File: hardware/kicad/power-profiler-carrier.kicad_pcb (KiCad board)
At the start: 4 copper layers, 160 x 100 mm, 309 parts, among them J1101 CPLD JTAG, J1201 Logic D0-D7, J201 JTAG, J202 3V3 GND, J301 USB-C power, J601 VIN, J801 VOUT, Q601 CSD17577Q3A, Q602 CSD17577Q3A, Q603 CSD17577Q3A, Q604 CSD17577Q3A, Q701 IRLML0030, Q702 IRLML0030, Q703 CSD17577Q3A, Q801 CSD17577Q3A, Q802 CSD17577Q3A, U1001 MCP6562-E/SN, U1002 MCP6561T-E/OT, U1101 EPM240T100C5N, U1201 SRV05-4, U1202 SRV05-4, U1203 SN74LVC8T245PW, U1301 MCP3208-BI/SL, U1302 MCP9700AT-E/TT, U201 ESP32-S3-DevKitC-1 N8R2/N16R2, U202 SN74LVC245APW, U301 LP5907MFX-3.3, U302 LP5907MFX-3.3, U401 LMR62014XMF, U402 LT3042EMSE, U403 LM27761DSG, U404 REF5025AID, U501 TPS63020DSJ, U502 OPA365AIDBV, U503 LT3080EDD, U504 MCP4921-E/SN, U505 OPA197IDBV, U601 TC4427EOA, U602 MCP6561T-E/OT, U701 TC4427EOA, U702 TC4427EOA, U703 MUX509IPWR, U801 OPA197IDBV, U901 AD8421ARZ, U902 OPA197IDBV, U903 OPA365AIDBV, U904 ADS8860IDGS

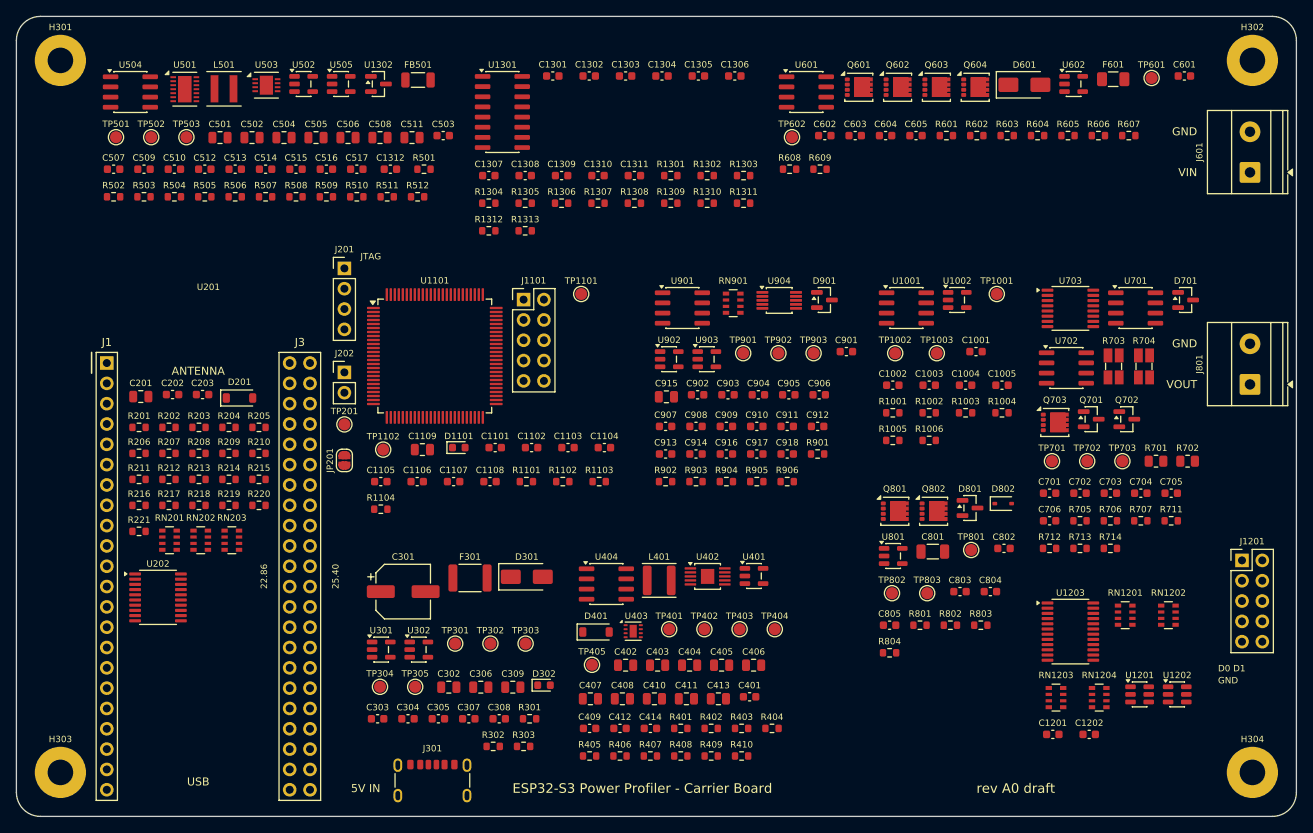
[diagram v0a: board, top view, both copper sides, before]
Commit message: feat(hardware): place the parts of draft A1 on a 130 mm x 100 mm board
The outline shrinks from 160 mm x 100 mm to 130 mm x 100 mm (D-46).
The back edge, on the left, has the Pico 2 with its USB connector and
the USB-C power connector. The front edge, on the right, has the logic
port and the two DUT connectors, each with the names of its pins.

The parts are no longer packed in rows. Each one stands near the pin
it serves, turned towards its connections, inside the area of its
functional block; the switching converters are in the left third and
the front end in the right third. The reference designators of 23
parts are hidden on the silkscreen, where no free place was left
beside the part, and three groups of parts lie just outside the
outline of their block.

Nothing is routed, and nobody has reviewed the placement for routing.
The design rules check reports no violation and no difference between
board and schematic; the unconnected items it lists are the missing
tracks.
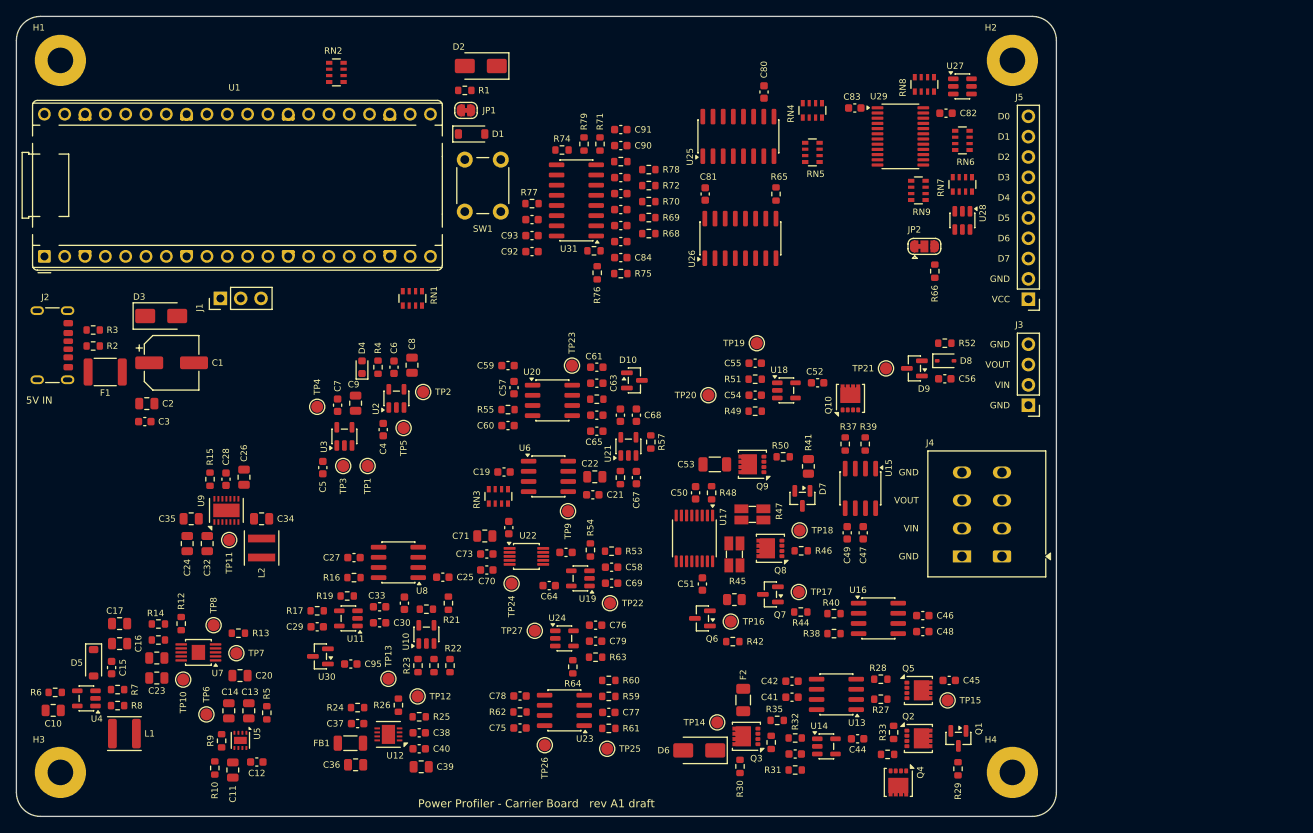
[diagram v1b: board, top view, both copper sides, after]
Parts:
- removed C1001, C1002, C1003, C1004, C1005, C1101, C1102, C1103, C1104, C1105, C1106, C1107, C1108, C1201, C1202, C1301, C1302, C1303, C1304, C1305, C1306, C1307, C1308, C1309, C1311, C1312, C202, C203, C303, C503, C507, C510, C512, C513, C514, C515, C516, C517, C602, C604, C702, C704, C705, C706, C802, C803, C804, C805, C901, C903, C909, C910, C913, C916: 100n, Capacitor_SMD:C_0603_1608Metric
- removed C1109, C201, C302, C306, C309, C413, C501, C502, C508, C511: 10u, Capacitor_SMD:C_0805_2012Metric
- removed C1310, C304, C305, C307, C308, C409, C414, C605, C904, C908, C917, C918: 1u, Capacitor_SMD:C_0603_1608Metric
- removed C301: 47u 16V, Capacitor_SMD:CP_Elec_6.3x5.4
- removed C401: 220p, Capacitor_SMD:C_0603_1608Metric
- removed C402, C405, C408, C410, C411: 4.7u, Capacitor_SMD:C_0805_2012Metric
- removed C403, C404, C406, C407: 4.7u 25V, Capacitor_SMD:C_0805_2012Metric
- removed C412, C509, C601, C701, C703, C902: 1u 25V, Capacitor_SMD:C_0603_1608Metric
- removed C504, C505, C506, C915: 22u, Capacitor_SMD:C_0805_2012Metric
- removed C603: 1n, Capacitor_SMD:C_0603_1608Metric
- removed C801: 100n C0G, Capacitor_SMD:C_1206_3216Metric
- removed C905: 1n C0G, Capacitor_SMD:C_0603_1608Metric
- removed C906, C907: 100p C0G, Capacitor_SMD:C_0603_1608Metric
- removed C911: 1.5n C0G, Capacitor_SMD:C_0603_1608Metric
- removed C912: 680p C0G, Capacitor_SMD:C_0603_1608Metric
- removed C914: 10n C0G, Capacitor_SMD:C_0603_1608Metric
- removed D1101: red, LED_SMD:LED_0603_1608Metric
- removed D201: B5819W, Diode_SMD:D_SOD-123
- removed D301: SMAJ5.0A, Diode_SMD:D_SMA
- removed D302: green, LED_SMD:LED_0603_1608Metric
- removed D401: MBR0530, Diode_SMD:D_SOD-123
- removed D601: SS34, Diode_SMD:D_SMA
- removed D701, D801, D901: BAV199, Package_TO_SOT_SMD:SOT-23
- removed D802: BZT52C5V6S, Diode_SMD:D_SOD-323
- removed F301: 2.5A hold, Fuse:Fuse_1812_4532Metric
- removed F601: 4A fast, Fuse:Fuse_1206_3216Metric
- removed FB501: 120R 3A, Inductor_SMD:L_1206_3216Metric
- removed H301, H302, H303, H304: M3, MountingHole:MountingHole_3.2mm_M3_Pad
- removed J1101: CPLD JTAG, Connector_PinHeader_2.54mm:PinHeader_2x05_P2.54mm_Vertical
- removed J1201: Logic D0-D7, Connector_PinHeader_2.54mm:PinHeader_2x05_P2.54mm_Vertical
- removed J201: JTAG, Connector_PinHeader_2.54mm:PinHeader_1x04_P2.54mm_Vertical
- removed J202: 3V3 GND, Connector_PinHeader_2.54mm:PinHeader_1x02_P2.54mm_Vertical
- removed J301: USB-C power, Connector_USB:USB_C_Receptacle_GCT_USB4125-xx-x_6P_TopMnt_Horizontal
- removed J601: VIN, TerminalBlock_Phoenix:TerminalBlock_Phoenix_MKDS-1,5-2-5.08_1x02_P5.08mm_Horizontal
- removed J801: VOUT, TerminalBlock_Phoenix:TerminalBlock_Phoenix_MKDS-1,5-2-5.08_1x02_P5.08mm_Horizontal
- removed JP201: 5V to devkit, Jumper:SolderJumper-2_P1.3mm_Open_RoundedPad1.0x1.5mm
- removed L401: 10u 1.3A, Inductor_SMD:L_Changjiang_FNR4020S
- removed L501: 1.5u 5A, Inductor_SMD:L_Coilcraft_XxL4020
- removed Q601, Q602, Q603, Q604, Q703, Q801, Q802: CSD17577Q3A, Package_SON:VSON-8_3.3x3.3mm_P0.65mm_NexFET
- removed Q701, Q702: IRLML0030, Package_TO_SOT_SMD:SOT-23
- removed R1001, R1004, R1005: 3.01k, Resistor_SMD:R_0603_1608Metric
- removed R1002, R1101, R1104, R1309, R206, R303, R508, R605, R606, R711, R712, R713, R714: 1k, Resistor_SMD:R_0603_1608Metric
- removed R1003: 34.8k, Resistor_SMD:R_0603_1608Metric
- removed R1006: 9.31k, Resistor_SMD:R_0603_1608Metric
- removed R1102, R1103, R1304, R1307, R1308, R1311, R217, R220, R221, R407, R510, R802, R803: 10k, Resistor_SMD:R_0603_1608Metric
- removed R1301, R1305, R607: 120k, Resistor_SMD:R_0603_1608Metric
- removed R1302, R1306, R1312, R210, R211, R212, R213, R214, R215, R216, R218, R219, R410, R608: 100k, Resistor_SMD:R_0603_1608Metric
- removed R1303: 110k, Resistor_SMD:R_0603_1608Metric
- removed R1310: 47k, Resistor_SMD:R_0603_1608Metric
- removed R1313: 200k, Resistor_SMD:R_0603_1608Metric
- removed R201, R202, R203, R204, R205, R207, R208, R209, R705, R706, R804: 47R, Resistor_SMD:R_0603_1608Metric
- removed R301, R302: 5.1k, Resistor_SMD:R_0603_1608Metric
- removed R401: 51k, Resistor_SMD:R_0603_1608Metric
- removed R402: 133k, Resistor_SMD:R_0603_1608Metric
- removed R403: 13.3k, Resistor_SMD:R_0603_1608Metric
- removed R404: 120k 0.1%, Resistor_SMD:R_0603_1608Metric
- removed R405: 442k, Resistor_SMD:R_0603_1608Metric
- removed R406: 12.4k, Resistor_SMD:R_0603_1608Metric
- removed R408: 2.2R, Resistor_SMD:R_0603_1608Metric
- removed R409: 226k, Resistor_SMD:R_0603_1608Metric
- removed R501: 470R, Resistor_SMD:R_0603_1608Metric
- removed R502, R505: 100k 0.1%, Resistor_SMD:R_0603_1608Metric
- removed R503: 121k 0.1%, Resistor_SMD:R_0603_1608Metric
- removed R504: 23.7k 0.1%, Resistor_SMD:R_0603_1608Metric
- removed R506: 20k 0.1%, Resistor_SMD:R_0603_1608Metric
- removed R507, R707: 10R, Resistor_SMD:R_0603_1608Metric
- removed R509: 4.3k, Resistor_SMD:R_0603_1608Metric
- removed R511: 10k 0.1%, Resistor_SMD:R_0603_1608Metric
- removed R512: 11k 0.1%, Resistor_SMD:R_0603_1608Metric
- removed R601, R603, R801, R906: 22R, Resistor_SMD:R_0603_1608Metric
- removed R602, R604: 1M, Resistor_SMD:R_0603_1608Metric
- removed R609: 2.2M, Resistor_SMD:R_0603_1608Metric
- removed R701: 1k 0.1%, Resistor_SMD:R_0805_2012Metric
- removed R702: 33R 0.1%, Resistor_SMD:R_0805_2012Metric
- removed R703: 1R 0.1%, Resistor_SMD:R_Shunt_Ohmite_LVK12
- removed R704: 0.1R 0.5%, Resistor_SMD:R_Shunt_Ohmite_LVK12
- removed R901: 523R 0.1%, Resistor_SMD:R_0603_1608Metric
- removed R902: 49.9k 0.1%, Resistor_SMD:R_0603_1608Metric
- removed R903: 1.02k 0.1%, Resistor_SMD:R_0603_1608Metric
- removed R904, R905: 3.9k, Resistor_SMD:R_0603_1608Metric
- removed RN1201, RN1202: 1k, Resistor_SMD:R_Array_Convex_4x0603
- removed RN1203, RN1204: 1M, Resistor_SMD:R_Array_Convex_4x0603
- removed RN201, RN202, RN203: 47R, Resistor_SMD:R_Array_Convex_4x0603
- removed RN901: 33R, Resistor_SMD:R_Array_Convex_4x0603
- removed TP1001: CMP_UP, TestPoint:TestPoint_Pad_D1.5mm
- removed TP1002: CMP_JUMP, TestPoint:TestPoint_Pad_D1.5mm
- removed TP1003: CMP_OC, TestPoint:TestPoint_Pad_D1.5mm
- removed TP1101: DBG0, TestPoint:TestPoint_Pad_D1.5mm
- removed TP1102: DBG1, TestPoint:TestPoint_Pad_D1.5mm
- removed TP201: +3V3_D, TestPoint:TestPoint_Pad_D1.5mm
- removed TP301: +5V, TestPoint:TestPoint_Pad_D1.5mm
- removed TP302: +3V3_C, TestPoint:TestPoint_Pad_D1.5mm
- removed TP303: +3V3_A, TestPoint:TestPoint_Pad_D1.5mm
- removed TP304, TP305, TP803: GND, TestPoint:TestPoint_Pad_D1.5mm
- removed TP401: +13V5, TestPoint:TestPoint_Pad_D1.5mm
- removed TP402: +12V_A, TestPoint:TestPoint_Pad_D1.5mm
- removed TP403: -4V_A, TestPoint:TestPoint_Pad_D1.5mm
- removed TP404: VREF, TestPoint:TestPoint_Pad_D1.5mm
- removed TP405: PWR_GOOD, TestPoint:TestPoint_Pad_D1.5mm
- removed TP501: V_PRE, TestPoint:TestPoint_Pad_D1.5mm
- removed TP502: LDO_OUT, TestPoint:TestPoint_Pad_D1.5mm
- removed TP503: LDO_SET, TestPoint:TestPoint_Pad_D1.5mm
- removed TP601: SUPPLY, TestPoint:TestPoint_Pad_D1.5mm
- removed TP602: VIN_P, TestPoint:TestPoint_Pad_D1.5mm
- removed TP701: G_R1, TestPoint:TestPoint_Pad_D1.5mm
- removed TP702: G_R2, TestPoint:TestPoint_Pad_D1.5mm
- removed TP703: G_R3, TestPoint:TestPoint_Pad_D1.5mm
- removed TP801: VOUT, TestPoint:TestPoint_Pad_D1.5mm
- removed TP802: GUARD, TestPoint:TestPoint_Pad_D1.5mm
- removed TP901: AMP_RAW, TestPoint:TestPoint_Pad_D1.5mm
- removed TP902: ADC_IN, TestPoint:TestPoint_Pad_D1.5mm
- removed TP903: PED, TestPoint:TestPoint_Pad_D1.5mm
- removed U1001: MCP6562-E/SN, Package_SO:SOIC-8_3.9x4.9mm_P1.27mm
- removed U1002, U602: MCP6561T-E/OT, Package_TO_SOT_SMD:SOT-23-5
- removed U1101: EPM240T100C5N, Package_QFP:LQFP-100_14x14mm_P0.5mm
- removed U1201, U1202: SRV05-4, Package_TO_SOT_SMD:SOT-23-6
- removed U1203: SN74LVC8T245PW, Package_SO:TSSOP-24_4.4x7.8mm_P0.65mm
- removed U1301: MCP3208-BI/SL, Package_SO:SOIC-16_3.9x9.9mm_P1.27mm
- removed U1302: MCP9700AT-E/TT, Package_TO_SOT_SMD:SOT-23
- removed U201: ESP32-S3-DevKitC-1 N8R2/N16R2, PowerProfiler:ESP32-S3-DevKitC-1_Socket
- removed U202: SN74LVC245APW, Package_SO:TSSOP-20_4.4x6.5mm_P0.65mm
- removed U301, U302: LP5907MFX-3.3, Package_TO_SOT_SMD:SOT-23-5
- removed U401: LMR62014XMF, Package_TO_SOT_SMD:SOT-23-5
- removed U402: LT3042EMSE, Package_SO:MSOP-10-1EP_3x3mm_P0.5mm_EP1.68x1.88mm
- removed U403: LM27761DSG, Package_SON:WSON-8-1EP_2x2mm_P0.5mm_EP0.9x1.6mm
- removed U404: REF5025AID, Package_SO:SOIC-8_3.9x4.9mm_P1.27mm
- removed U501: TPS63020DSJ, Package_DFN_QFN:DFN-14-1EP_3x4mm_P0.5mm_EP1.7x3.3mm
- removed U502, U903: OPA365AIDBV, Package_TO_SOT_SMD:SOT-23-5
- removed U503: LT3080EDD, Package_DFN_QFN:DFN-8-1EP_3x3mm_P0.5mm_EP1.66x2.38mm
- removed U504: MCP4921-E/SN, Package_SO:SOIC-8_3.9x4.9mm_P1.27mm
- removed U505, U801, U902: OPA197IDBV, Package_TO_SOT_SMD:SOT-23-5
- removed U601, U701, U702: TC4427EOA, Package_SO:SOIC-8_3.9x4.9mm_P1.27mm
- removed U703: MUX509IPWR, Package_SO:TSSOP-16_4.4x5mm_P0.65mm
- removed U901: AD8421ARZ, Package_SO:SOIC-8_3.9x4.9mm_P1.27mm
- removed U904: ADS8860IDGS, Package_SO:MSOP-10_3x3mm_P0.5mm
- added C1: 47u 16V, Capacitor_SMD:CP_Elec_6.3x5.4, F.Cu at (69.4, 93.3)
- added C10: 4.7u, Capacitor_SMD:C_0805_2012Metric, F.Cu at (54.6, 136.8)
- added C11: 4.7u, Capacitor_SMD:C_0805_2012Metric, F.Cu at (77.0, 144.2)
- added C12: 1u, Capacitor_SMD:C_0603_1608Metric, F.Cu at (80.0, 143.2)
- added C13: 4.7u, Capacitor_SMD:C_0805_2012Metric, F.Cu at (79.0, 136.8)
- added C14: 4.7u, Capacitor_SMD:C_0805_2012Metric, F.Cu at (76.5, 136.8)
- added C15: 220p, Capacitor_SMD:C_0603_1608Metric, F.Cu at (61.9, 131.4)
- added C16: 4.7u 25V, Capacitor_SMD:C_0805_2012Metric, F.Cu at (62.9, 128.4)
- added C17: 4.7u 25V, Capacitor_SMD:C_0805_2012Metric, F.Cu at (62.9, 125.9)
- added C18: 4.7u, Capacitor_SMD:C_0805_2012Metric, F.Cu at (67.5, 130.2)
- added C19: 1u 25V, Capacitor_SMD:C_0603_1608Metric, F.Cu at (111.0, 107.0)
- added C2: 10u, Capacitor_SMD:C_0805_2012Metric, F.Cu at (66.3, 98.4)
- added C20: 4.7u 25V, Capacitor_SMD:C_0805_2012Metric, F.Cu at (78.0, 132.4)
- added C21: 1u, Capacitor_SMD:C_0603_1608Metric, F.Cu at (122.0, 109.8)
- added C22: 10u, Capacitor_SMD:C_0805_2012Metric, F.Cu at (122.3, 107.5)
- added C23: 4.7u 25V, Capacitor_SMD:C_0805_2012Metric, F.Cu at (67.5, 132.7)
- added C24: 10u, Capacitor_SMD:C_0805_2012Metric, F.Cu at (71.3, 115.9)
- added C25: 100n, Capacitor_SMD:C_0603_1608Metric, F.Cu at (103.3, 120.1)
- added C26: 10u, Capacitor_SMD:C_0805_2012Metric, F.Cu at (78.5, 107.6)
- added C27: 100n, Capacitor_SMD:C_0603_1608Metric, F.Cu at (92.2, 117.7)
- added C28: 100n, Capacitor_SMD:C_0603_1608Metric, F.Cu at (76.2, 107.8)
- added C29: 100n, Capacitor_SMD:C_0603_1608Metric, F.Cu at (87.6, 126.3)
- added C3: 100n, Capacitor_SMD:C_0603_1608Metric, F.Cu at (66.0, 100.7)
- added C30: 100n, Capacitor_SMD:C_0603_1608Metric, F.Cu at (95.4, 125.8)
- added C31: 100n, Capacitor_SMD:C_0603_1608Metric, F.Cu at (98.5, 123.3)
- added C32: 22u, Capacitor_SMD:C_0805_2012Metric, F.Cu at (73.8, 115.9)
- added C33: 100n, Capacitor_SMD:C_0603_1608Metric, F.Cu at (95.4, 123.8)
- added C34: 22u, Capacitor_SMD:C_0805_2012Metric, F.Cu at (80.7, 112.8)
- added C35: 22u, Capacitor_SMD:C_0805_2012Metric, F.Cu at (71.8, 112.8)
- added C36: 10u, Capacitor_SMD:C_0805_2012Metric, F.Cu at (92.4, 143.6)
- added C37: 1u 25V, Capacitor_SMD:C_0603_1608Metric, F.Cu at (92.7, 138.4)
- added C38: 100n, Capacitor_SMD:C_0603_1608Metric, F.Cu at (100.3, 139.6)
- added C39: 10u, Capacitor_SMD:C_0805_2012Metric, F.Cu at (100.6, 143.8)
- added C4: 1u, Capacitor_SMD:C_0603_1608Metric, F.Cu at (95.8, 101.7)
- added C40: 100n, Capacitor_SMD:C_0603_1608Metric, F.Cu at (100.3, 141.6)
- added C41: 1u 25V, Capacitor_SMD:C_0603_1608Metric, F.Cu at (146.9, 135.1)
- added C42: 100n, Capacitor_SMD:C_0603_1608Metric, F.Cu at (146.9, 133.1)
- added C43: 1n, Capacitor_SMD:C_0603_1608Metric, F.Cu at (147.3, 142.2)
- added C44: 100n, Capacitor_SMD:C_0603_1608Metric, F.Cu at (155.2, 140.3)
- added C45: 1u, Capacitor_SMD:C_0603_1608Metric, F.Cu at (166.6, 133.0)
- added C46: 1u 25V, Capacitor_SMD:C_0603_1608Metric, F.Cu at (163.3, 124.9)
- added C47: 100n, Capacitor_SMD:C_0603_1608Metric, F.Cu at (155.8, 114.5)
- added C48: 1u 25V, Capacitor_SMD:C_0603_1608Metric, F.Cu at (163.3, 126.9)
- added C49: 100n, Capacitor_SMD:C_0603_1608Metric, F.Cu at (153.8, 114.5)
- added C5: 1u, Capacitor_SMD:C_0603_1608Metric, F.Cu at (88.3, 106.4)
- added C50: 100n, Capacitor_SMD:C_0603_1608Metric, F.Cu at (134.9, 109.5)
- added C51: 100n, Capacitor_SMD:C_0603_1608Metric, F.Cu at (135.8, 121.0)
- added C52: 100n, Capacitor_SMD:C_0603_1608Metric, F.Cu at (150.2, 95.8)
- added C53: 100n C0G, Capacitor_SMD:C_1206_3216Metric, F.Cu at (137.3, 106.0)
- added C54: 100n, Capacitor_SMD:C_0603_1608Metric, F.Cu at (142.3, 97.3)
- added C55: 100n, Capacitor_SMD:C_0603_1608Metric, F.Cu at (142.3, 93.3)
- added C56: 100n, Capacitor_SMD:C_0603_1608Metric, F.Cu at (166.1, 95.3)
- added C57: 1n C0G, Capacitor_SMD:C_0603_1608Metric, F.Cu at (112.2, 96.4)
- added C58: 1u, Capacitor_SMD:C_0603_1608Metric, F.Cu at (124.4, 118.8)
- added C59: 100p C0G, Capacitor_SMD:C_0603_1608Metric, F.Cu at (111.5, 93.7)
- added C6: 1u, Capacitor_SMD:C_0603_1608Metric, F.Cu at (97.2, 93.8)
- added C60: 100p C0G, Capacitor_SMD:C_0603_1608Metric, F.Cu at (111.5, 101.2)
- added C61: 100n, Capacitor_SMD:C_0603_1608Metric, F.Cu at (122.5, 93.8)
- added C62: 100n, Capacitor_SMD:C_0603_1608Metric, F.Cu at (122.5, 99.8)
- added C63: 1u 25V, Capacitor_SMD:C_0603_1608Metric, F.Cu at (122.5, 95.8)
- added C64: 100n, Capacitor_SMD:C_0603_1608Metric, F.Cu at (116.6, 121.2)
- added C65: 1u, Capacitor_SMD:C_0603_1608Metric, F.Cu at (122.5, 101.8)
- added C66: 100n, Capacitor_SMD:C_0603_1608Metric, F.Cu at (125.5, 99.8)
- added C67: 680p C0G, Capacitor_SMD:C_0603_1608Metric, F.Cu at (127.5, 107.7)
- added C68: 1.5n C0G, Capacitor_SMD:C_0603_1608Metric, F.Cu at (127.5, 99.8)
- added C69: 100n, Capacitor_SMD:C_0603_1608Metric, F.Cu at (124.4, 120.8)
- added C7: 1u, Capacitor_SMD:C_0603_1608Metric, F.Cu at (90.2, 98.6)
- added C70: 10n C0G, Capacitor_SMD:C_0603_1608Metric, F.Cu at (108.8, 119.2)
- added C71: 22u, Capacitor_SMD:C_0805_2012Metric, F.Cu at (108.5, 115.0)
- added C72: 100n, Capacitor_SMD:C_0603_1608Metric, F.Cu at (111.5, 113.9)
- added C73: 1u, Capacitor_SMD:C_0603_1608Metric, F.Cu at (108.8, 117.2)
- added C74: 1u, Capacitor_SMD:C_0603_1608Metric, F.Cu at (118.7, 117.0)
- added C75: 100n, Capacitor_SMD:C_0603_1608Metric, F.Cu at (113.0, 138.9)
- added C76: 100n, Capacitor_SMD:C_0603_1608Metric, F.Cu at (122.4, 126.1)
- added C77: 100n, Capacitor_SMD:C_0603_1608Metric, F.Cu at (124.0, 137.0)
- added C78: 100n, Capacitor_SMD:C_0603_1608Metric, F.Cu at (113.0, 134.9)
- added C79: 100n, Capacitor_SMD:C_0603_1608Metric, F.Cu at (122.4, 128.1)
- added C8: 10u, Capacitor_SMD:C_0805_2012Metric, F.Cu at (99.5, 93.6)
- added C80: 100n, Capacitor_SMD:C_0603_1608Metric, F.Cu at (143.4, 59.5)
- added C81: 100n, Capacitor_SMD:C_0603_1608Metric, F.Cu at (136.1, 72.2)
- added C82: 100n, Capacitor_SMD:C_0603_1608Metric, F.Cu at (166.2, 62.1)
- added C83: 100n, Capacitor_SMD:C_0603_1608Metric, F.Cu at (154.8, 61.5)
- added C84: 100n, Capacitor_SMD:C_0603_1608Metric, F.Cu at (125.5, 80.2)
- added C85: 100n, Capacitor_SMD:C_0603_1608Metric, F.Cu at (125.5, 78.2)
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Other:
- board size 160 x 100 mm -> 130 x 100 mm
- board text added: "Controller"
- board text added: "D0"
- board text added: "D1"
- board text added: "D2"
- board text added: "D3"
- board text added: "D4"
- board text added: "D5"
- board text added: "D6"
- board text added: "D7"
- board text added: "Logic inputs"
- board text added: "Mode switches"
- board text added: "Power Profiler - Carrier Board rev A1 draft"
- board text added: "Pre-regulator"
- board text added: "Side data"
- board text added: "VCC"
- board text removed: "D0 D1"
- board text removed: "Digital inputs"
- board text removed: "ESP32-S3 Power Profiler - Carrier Board"
- board text removed: "JTAG"
- board text removed: "Path switching"
- board text removed: "Range logic"
- board text removed: "rev A0 draft"

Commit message: feat(hardware): place and route draft A2 on a 150 mm x 100 mm board
The outline grows from 130 mm x 100 mm to 150 mm x 100 mm (D-85). A
script places the 425 footprints inside the areas of sixteen functional
blocks, with the front end under the frame of a shield can, and an
autorouter draws the tracks (D-86): 956 of the 984 connections, on
three layers over an unbroken ground plane. 28 connections are open.

The project file holds thirteen net classes, the default class among
them, and a rule file adds the clearances that a net class cannot
express. The stackup is the build that section 10.1 of the
specification assumes until a manufacturer is chosen.

The design rules check reports no rule violation and no difference
between board and schematic; its 28 unconnected items are the open
connections. The board is an autorouted draft that needs a layout
review before fabrication: the pours of the 1 A path, the guard ring,
the sense pairs and the loops of the switching converters are not
drawn.
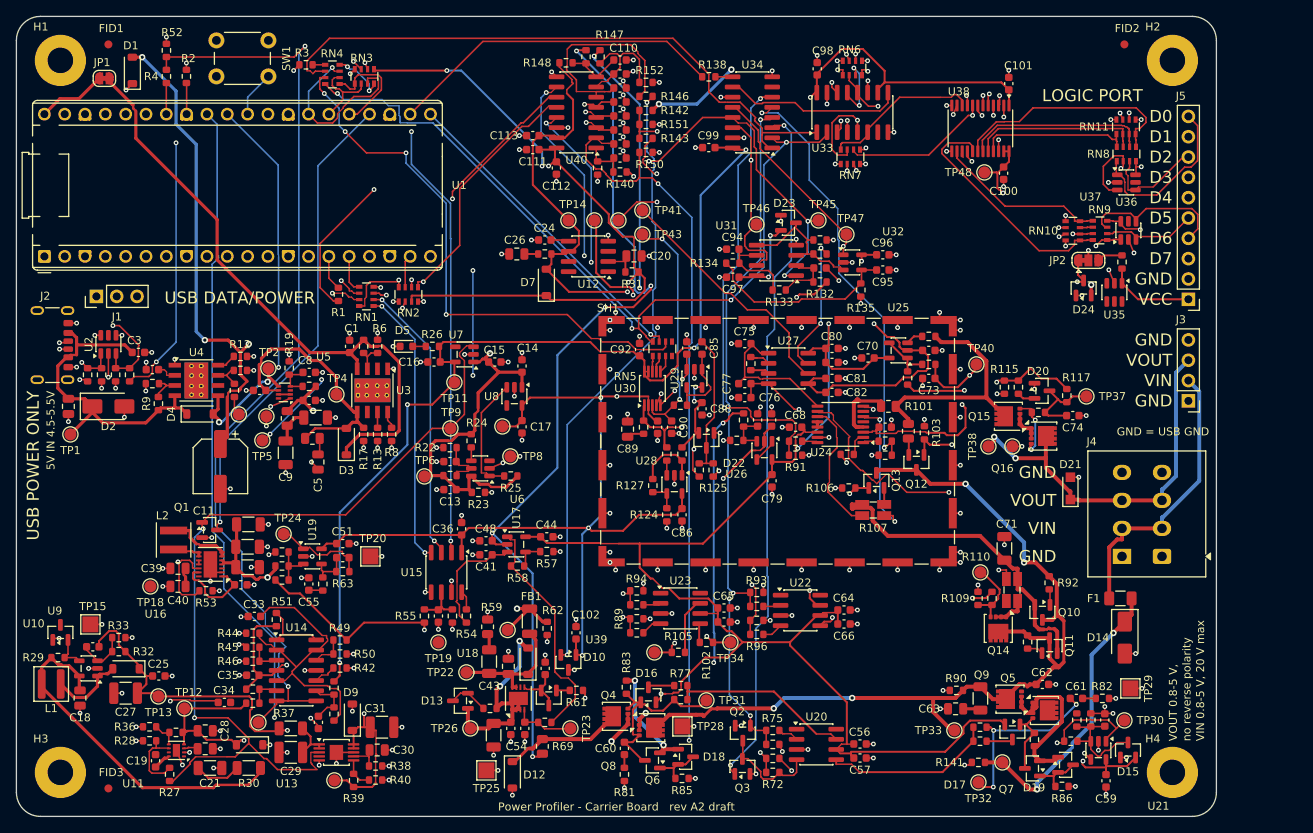
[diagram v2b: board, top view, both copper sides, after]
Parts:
- removed F2: 4A fast, Fuse:Fuse_1206_3216Metric
- added C100: 100n 50V X7R, Capacitor_SMD:C_0603_1608Metric, F.Cu at (173.4, 69.6)
- added C101: 100n 50V X7R, Capacitor_SMD:C_0603_1608Metric, F.Cu at (174.1, 58.4)
- added C102: 100n 50V X7R, Capacitor_SMD:C_0603_1608Metric, F.Cu at (120.0, 127.0)
- added C103: 100n 50V X7R, Capacitor_SMD:C_0603_1608Metric, F.Cu at (125.5, 67.7)
- added C104: 100n 50V X7R, Capacitor_SMD:C_0603_1608Metric, F.Cu at (125.5, 66.0)
- added C105: 100n 50V X7R, Capacitor_SMD:C_0603_1608Metric, F.Cu at (125.5, 64.2)
- added C106: 100n 50V X7R, Capacitor_SMD:C_0603_1608Metric, F.Cu at (125.5, 62.5)
- added C107: 100n 50V X7R, Capacitor_SMD:C_0603_1608Metric, F.Cu at (125.5, 60.7)
- added C108: 100n 50V X7R, Capacitor_SMD:C_0603_1608Metric, F.Cu at (125.5, 59.0)
- added C109: 100n 50V X7R, Capacitor_SMD:C_0603_1608Metric, F.Cu at (125.5, 57.2)
- added C110: 100n 50V X7R, Capacitor_SMD:C_0603_1608Metric, F.Cu at (125.5, 55.5)
- added C111: 100n 50V X7R, Capacitor_SMD:C_0603_1608Metric, F.Cu at (114.5, 66.7)
- added C112: 1u 25V X7R, Capacitor_SMD:C_0603_1608Metric, F.Cu at (117.5, 69.0)
- added C113: 100n 50V X7R, Capacitor_SMD:C_0603_1608Metric, F.Cu at (114.5, 64.9)
- added C96: 100n 50V X7R, Capacitor_SMD:C_0603_1608Metric, F.Cu at (158.3, 79.8)
- added C97: 100n 50V X7R, Capacitor_SMD:C_0603_1608Metric, F.Cu at (139.6, 82.6)
- added C98: 100n 50V X7R, Capacitor_SMD:C_0603_1608Metric, F.Cu at (150.1, 56.5)
- added C99: 100n 50V X7R, Capacitor_SMD:C_0603_1608Metric, F.Cu at (136.6, 66.4)
- added D11: 1N5819HW, Diode_SMD:D_SOD-123, F.Cu at (114.0, 130.6)
- added D12: 1N5819HW, Diode_SMD:D_SOD-123, F.Cu at (112.0, 144.8)
- added D13: BAV199, Package_TO_SOT_SMD:SOT-23, F.Cu at (105.5, 135.6)
- added D14: SMAJ20CA, Diode_SMD:D_SMA, F.Cu at (188.6, 127.7)
- added D15: BAV199, Package_TO_SOT_SMD:SOT-23, F.Cu at (188.9, 141.7)
- added D16: BAV199, Package_TO_SOT_SMD:SOT-23, F.Cu at (129.0, 134.8)
- added D17: BAV199, Package_TO_SOT_SMD:SOT-23, F.Cu at (174.5, 139.4)
- added D18: BAV199, Package_TO_SOT_SMD:SOT-23, F.Cu at (133.7, 142.6)
- added D19: BAV199, Package_TO_SOT_SMD:SOT-23, F.Cu at (181.2, 143.6)
- added D20: BAV199, Package_TO_SOT_SMD:SOT-23, F.Cu at (178.2, 96.8)
- added D21: PTVS15VS1UR, Diode_SMD:Nexperia_CFP3_SOD-123W, F.Cu at (181.8, 109.0)
- added D22: BAV199, Package_TO_SOT_SMD:SOT-23, F.Cu at (136.2, 103.0)
- added D23: BAV199, Package_TO_SOT_SMD:SOT-23, F.Cu at (146.5, 75.8)
- added D24: BAT54S, Package_TO_SOT_SMD:SOT-23, F.Cu at (183.4, 84.0)
- added FID1: Fiducial, Fiducial:Fiducial_1mm_Mask2mm, F.Cu at (61.5, 53.5)
- added FID2: Fiducial, Fiducial:Fiducial_1mm_Mask2mm, F.Cu at (188.5, 53.5)
- added FID3: Fiducial, Fiducial:Fiducial_1mm_Mask2mm, F.Cu at (61.5, 146.5)
- added Q11: IRLML0030, Package_TO_SOT_SMD:SOT-23, F.Cu at (179.2, 128.7)
- added Q12: IRLML0030, Package_TO_SOT_SMD:SOT-23, F.Cu at (162.5, 105.8)
- added Q13: IRLML0030, Package_TO_SOT_SMD:SOT-23, F.Cu at (157.5, 108.0)
- added Q14: CSD17577Q3A, Package_SON:VSON-8_3.3x3.3mm_P0.65mm_NexFET, F.Cu at (172.8, 126.5)
- added Q15: CSD17577Q3A, Package_SON:VSON-8_3.3x3.3mm_P0.65mm_NexFET, F.Cu at (174.0, 100.0)
- added Q16: CSD17577Q3A, Package_SON:VSON-8_3.3x3.3mm_P0.65mm_NexFET, F.Cu at (178.3, 102.5)
- added R100: 22R 1%, Resistor_SMD:R_0603_1608Metric, F.Cu at (176.4, 128.2)
- added R101: 1k 0.1% 25ppm, Resistor_SMD:R_0805_2012Metric, F.Cu at (159.0, 98.8)
- added R102: 47R 1%, Resistor_SMD:R_0603_1608Metric, F.Cu at (136.2, 128.2)
- added R103: 100k 1%, Resistor_SMD:R_0603_1608Metric, F.Cu at (163.5, 102.0)
- added R104: 33R 0.1% 25ppm, Resistor_SMD:R_0805_2012Metric, F.Cu at (161.5, 101.8)
- added R105: 47R 1%, Resistor_SMD:R_0603_1608Metric, F.Cu at (132.8, 129.5)
- added R106: 100k 1%, Resistor_SMD:R_0603_1608Metric, F.Cu at (154.1, 109.0)
- added R107: 1R 0.5% 25ppm, Resistor_SMD:R_Shunt_Ohmite_LVK12, F.Cu at (157.1, 111.7)
- added R108: 10R 1%, Resistor_SMD:R_0603_1608Metric, F.Cu at (171.9, 122.8)
- added R109: 100k 1%, Resistor_SMD:R_0603_1608Metric, F.Cu at (170.2, 122.8)
- added R110: 0.1R 0.25% 50ppm, Resistor_SMD:R_Shunt_Ohmite_LVK12, F.Cu at (174.4, 121.7)
- added R111: 1k 1%, Resistor_SMD:R_0603_1608Metric, F.Cu at (147.4, 103.1)
- added R112: 1k 1%, Resistor_SMD:R_0603_1608Metric, F.Cu at (158.6, 103.1)
- added R113: 10k 1%, Resistor_SMD:R_0603_1608Metric, F.Cu at (153.8, 104.8)
- added R114: 10k 1%, Resistor_SMD:R_0603_1608Metric, F.Cu at (164.1, 90.0)
- added R115: 100k 1%, Resistor_SMD:R_0603_1608Metric, F.Cu at (173.5, 96.3)
- added R116: 220R 1%, Resistor_SMD:R_0603_1608Metric, F.Cu at (175.2, 96.3)
- added R117: 2.2M 1%, Resistor_SMD:R_0603_1608Metric, F.Cu at (181.3, 97.4)
- added R118: 1k 1%, Resistor_SMD:R_0603_1608Metric, F.Cu at (161.4, 95.2)
- added R119: 47R 1%, Resistor_SMD:R_0603_1608Metric, F.Cu at (164.1, 93.5)
- added R120: 10R 1%, Resistor_SMD:R_0603_1608Metric, F.Cu at (177.8, 99.5)
- added R121: 49.9k 0.1% 25ppm, Resistor_SMD:R_0603_1608Metric, F.Cu at (140.9, 100.5)
- added R122: 1.02k 0.1% 25ppm, Resistor_SMD:R_0603_1608Metric, F.Cu at (140.1, 103.0)
- added R123: 523R 0.1% 25ppm, Resistor_SMD:R_0603_1608Metric, F.Cu at (141.8, 93.4)
- added R124: 11k 0.1% 25ppm, Resistor_SMD:R_0603_1608Metric, F.Cu at (131.3, 112.3)
- added R125: 3.9k 1%, Resistor_SMD:R_0603_1608Metric, F.Cu at (137.1, 106.7)
- added R126: 10k 1%, Resistor_SMD:R_0603_1608Metric, F.Cu at (131.3, 104.7)
- added R127: 1k 0.1% 25ppm, Resistor_SMD:R_0603_1608Metric, F.Cu at (129.6, 108.7)
- added R128: 3.9k 1%, Resistor_SMD:R_0603_1608Metric, F.Cu at (135.3, 106.7)
- added R129: 10R 1%, Resistor_SMD:R_0603_1608Metric, F.Cu at (133.2, 104.7)
- added R130: 22R 1%, Resistor_SMD:R_0603_1608Metric, F.Cu at (133.0, 98.6)
- added R131: 0.22R 1%, Resistor_SMD:R_0603_1608Metric, F.Cu at (128.4, 101.3)
- added R132: 34.8k 0.1% 25ppm, Resistor_SMD:R_0603_1608Metric, F.Cu at (150.4, 83.2)
- added R133: 3.6k 0.1% 25ppm, Resistor_SMD:R_0603_1608Metric, F.Cu at (145.3, 84.2)
- added R134: 2.4k 0.1% 25ppm, Resistor_SMD:R_0603_1608Metric, F.Cu at (139.6, 80.8)
- added R135: 9.31k 0.1% 25ppm, Resistor_SMD:R_0603_1608Metric, F.Cu at (155.6, 84.2)
- added R136: 3.01k 0.1% 25ppm, Resistor_SMD:R_0603_1608Metric, F.Cu at (150.4, 79.7)
- added R137: 1k 0.1% 25ppm, Resistor_SMD:R_0603_1608Metric, F.Cu at (150.4, 78.0)
- added R138: 33R 1%, Resistor_SMD:R_0603_1608Metric, F.Cu at (136.6, 57.5)
- added R139: 100R 1%, Resistor_SMD:R_0603_1608Metric, F.Cu at (188.2, 80.7)
- added R140: 120k 1%, Resistor_SMD:R_0603_1608Metric, F.Cu at (125.5, 69.5)
- added R141: 430k 1%, Resistor_SMD:R_0603_1608Metric, F.Cu at (170.2, 143.2)
- added R142: 120k 1%, Resistor_SMD:R_0603_1608Metric, F.Cu at (128.7, 61.8)
- added R143: 68.1k 1%, Resistor_SMD:R_0603_1608Metric, F.Cu at (128.7, 65.2)
- added R144: 10k 1%, Resistor_SMD:R_0603_1608Metric, F.Cu at (58.9, 94.8)
- added R145: 10k 1%, Resistor_SMD:R_0603_1608Metric, F.Cu at (64.2, 94.8)
- added R146: 1k 1%, Resistor_SMD:R_0603_1608Metric, F.Cu at (128.7, 60.0)
- added R147: 47k 1%, Resistor_SMD:R_0603_1608Metric, F.Cu at (123.0, 55.0)
- added R148: 100k 1%, Resistor_SMD:R_0603_1608Metric, F.Cu at (118.7, 55.8)
- added R149: 100k 1%, Resistor_SMD:R_0603_1608Metric, F.Cu at (122.7, 69.0)
- added R150: 10k 1%, Resistor_SMD:R_0603_1608Metric, F.Cu at (128.7, 67.0)
- added R151: 100k 1%, Resistor_SMD:R_0603_1608Metric, F.Cu at (128.7, 63.5)
- added R152: 10k 1%, Resistor_SMD:R_0603_1608Metric, F.Cu at (128.7, 58.2)
- added R153: 200k 1%, Resistor_SMD:R_0603_1608Metric, F.Cu at (121.2, 55.0)
- added R80: 100k 1%, Resistor_SMD:R_0603_1608Metric, F.Cu at (170.4, 138.8)
- added R81: 6.8k 1%, Resistor_SMD:R_0603_1608Metric, F.Cu at (126.0, 144.8)
- added R82: 6.8k 1%, Resistor_SMD:R_0603_1608Metric, F.Cu at (185.8, 135.2)
- added R83: 2.2M 1%, Resistor_SMD:R_0603_1608Metric, F.Cu at (126.2, 133.8)
- added R84: 2.2M 1%, Resistor_SMD:R_0603_1608Metric, F.Cu at (177.2, 140.4)
- added R85: 100k 1%, Resistor_SMD:R_0603_1608Metric, F.Cu at (133.2, 145.2)
- added R86: 100k 1%, Resistor_SMD:R_0603_1608Metric, F.Cu at (180.7, 146.2)
- added R87: 0.47R 1% 0.5W, Resistor_SMD:R_1206_3216Metric, F.Cu at (170.5, 135.2)
- added R88: 1k 1%, Resistor_SMD:R_0603_1608Metric, F.Cu at (142.6, 125.5)
- added R89: 1k 1%, Resistor_SMD:R_0603_1608Metric, F.Cu at (127.5, 125.3)
- added R90: 100k 1%, Resistor_SMD:R_0603_1608Metric, F.Cu at (167.5, 134.2)
- added R91: 5.1k 1%, Resistor_SMD:R_0603_1608Metric, F.Cu at (147.4, 104.8)
- added R92: 22R 1%, Resistor_SMD:R_0603_1608Metric, F.Cu at (179.1, 120.8)
- added R93: 1k 1%, Resistor_SMD:R_0603_1608Metric, F.Cu at (142.6, 122.0)
- added R94: 1k 1%, Resistor_SMD:R_0603_1608Metric, F.Cu at (127.5, 121.8)
- added R95: 5.1k 1%, Resistor_SMD:R_0603_1608Metric, F.Cu at (158.6, 104.8)
- added R96: 1k 1%, Resistor_SMD:R_0603_1608Metric, F.Cu at (142.6, 127.2)
- added R97: 1k 1%, Resistor_SMD:R_0603_1608Metric, F.Cu at (127.5, 127.0)
- added R98: 1k 1%, Resistor_SMD:R_0603_1608Metric, F.Cu at (142.6, 123.8)
- added R99: 1k 1%, Resistor_SMD:R_0603_1608Metric, F.Cu at (127.5, 123.5)
- added RN10: 470k, Resistor_SMD:R_Array_Convex_4x0603, F.Cu at (182.1, 76.8)
- added RN11: 470k, Resistor_SMD:R_Array_Convex_4x0603, F.Cu at (188.7, 63.8)
- added SH1: BMI-S-210-F, RF_Shielding:Laird_Technologies_BMI-S-210-F_44.00x30.50mm, F.Cu at (145.2, 103.1)
- added TP28: GND, TestPoint:TestPoint_Pad_2.0x2.0mm, F.Cu at (133.2, 138.8)
- added TP29: GND, TestPoint:TestPoint_Pad_2.0x2.0mm, F.Cu at (189.2, 134.0)
- added TP30: VIN_OV, TestPoint:TestPoint_Pad_D1.5mm, F.Cu at (188.5, 138.0)
- added TP31: SRC_G, TestPoint:TestPoint_Pad_D1.5mm, F.Cu at (136.2, 135.5)
- added TP32: AMP_G, TestPoint:TestPoint_Pad_D1.5mm, F.Cu at (170.2, 145.8)
- added TP33: SUPPLY, TestPoint:TestPoint_Pad_D1.5mm, F.Cu at (167.2, 139.2)
- added TP34: G_R1, TestPoint:TestPoint_Pad_D1.5mm, F.Cu at (139.2, 128.2)
- added TP35: G_R2, TestPoint:TestPoint_Pad_D1.5mm, F.Cu at (129.8, 129.5)
- added TP36: G_R3, TestPoint:TestPoint_Pad_D1.5mm, F.Cu at (170.5, 119.5)
- added TP37: OUT_GATE, TestPoint:TestPoint_Pad_D1.5mm, F.Cu at (183.8, 97.5)
- added TP38: VOUT, TestPoint:TestPoint_Pad_D1.5mm, F.Cu at (171.5, 103.8)
- added TP39: GND, TestPoint:TestPoint_Pad_D1.5mm, F.Cu at (174.5, 103.8)
- added TP40: GUARD, TestPoint:TestPoint_Pad_D1.5mm, F.Cu at (170.0, 93.5)
- added TP41: PED, TestPoint:TestPoint_Pad_D1.5mm, F.Cu at (128.2, 74.2)
- added TP42: VDRV, TestPoint:TestPoint_Pad_D1.5mm, F.Cu at (122.2, 75.5)
- added TP43: ADC_IN, TestPoint:TestPoint_Pad_D1.5mm, F.Cu at (128.2, 77.2)
- added TP44: AMP_RAW, TestPoint:TestPoint_Pad_D1.5mm, F.Cu at (125.2, 75.5)
- added TP45: CMP_JUMP, TestPoint:TestPoint_Pad_D1.5mm, F.Cu at (150.2, 75.5)
- added TP46: CMP_OC, TestPoint:TestPoint_Pad_D1.5mm, F.Cu at (142.5, 76.0)
- added TP47: CMP_UP, TestPoint:TestPoint_Pad_D1.5mm, F.Cu at (153.8, 77.2)
- added TP48: VCC_B, TestPoint:TestPoint_Pad_D1.5mm, F.Cu at (171.0, 69.5)
- added U32: MCP6561T-E/OT, Package_TO_SOT_SMD:SOT-23-5, F.Cu at (154.5, 80.8)
- added U33: SN74LV165ADR, Package_SO:SOIC-16_3.9x9.9mm_P1.27mm, F.Cu at (154.5, 62.0)
- added U34: SN74LV165ADR, Package_SO:SOIC-16_3.9x9.9mm_P1.27mm, F.Cu at (142.0, 62.0)
- added U35: TPD4E1U06DBVR, Package_TO_SOT_SMD:SOT-23-6, F.Cu at (187.2, 84.5)
- added U36: TPD4E1U06DBVR, Package_TO_SOT_SMD:SOT-23-6, F.Cu at (188.8, 70.8)
- added U37: TPD4E1U06DBVR, Package_TO_SOT_SMD:SOT-23-6, F.Cu at (189.0, 76.8)
- added U38: SN74LVC8T245PW, Package_SO:TSSOP-24_4.4x7.8mm_P0.65mm, F.Cu at (170.5, 64.0)
- added U39: MCP9700AT-E/TT, Package_TO_SOT_SMD:SOT-23, F.Cu at (119.0, 130.8)
- added U40: MCP3208-BI/SL, Package_SO:SOIC-16_3.9x9.9mm_P1.27mm, F.Cu at (120.0, 62.0)
- C1: value 47u 16V -> 100n 50V X7R; footprint Capacitor_SMD:CP_Elec_6.3x5.4 -> Capacitor_SMD:C_0603_1608Metric
- C10: value 4.7u -> 22u 10V X7R; footprint Capacitor_SMD:C_0805_2012Metric -> Capacitor_SMD:C_1206_3216Metric
- C11: value 4.7u -> 47u 16V; footprint Capacitor_SMD:C_0805_2012Metric -> Capacitor_SMD:CP_Elec_6.3x5.4
- C12, C58: value 1u -> 1n 50V C0G
- C13: value 4.7u -> 100n 50V X7R; footprint Capacitor_SMD:C_0805_2012Metric -> Capacitor_SMD:C_0603_1608Metric
- C14: value 4.7u -> 1u 25V X7R; footprint Capacitor_SMD:C_0805_2012Metric -> Capacitor_SMD:C_0603_1608Metric
- C15: value 220p -> 1u 25V X7R
- C16, C17: value 4.7u 25V -> 1u 25V X7R; footprint Capacitor_SMD:C_0805_2012Metric -> Capacitor_SMD:C_0603_1608Metric
- C18: value 4.7u -> 4.7u 25V X7R
- C19, C41: value 1u 25V -> 1u 25V X7R
- C2, C22: value 10u -> 4.7u 25V X7R
- C20: value 4.7u 25V -> 4.7u 25V X7R
- C21: value 1u -> 22u 10V X7R; footprint Capacitor_SMD:C_0603_1608Metric -> Capacitor_SMD:C_1206_3216Metric
- C23: value 4.7u 25V -> 220p 50V C0G; footprint Capacitor_SMD:C_0805_2012Metric -> Capacitor_SMD:C_0603_1608Metric
- C24: value 10u -> 1u 25V X7R; footprint Capacitor_SMD:C_0805_2012Metric -> Capacitor_SMD:C_0603_1608Metric
- C25, C3, C38, C44, C49, C51, C54, C55, C61, C66, C69, C72, C79, C80, C81, C84, C86, C88, C94, C95: value 100n -> 100n 50V X7R
- C26: value 10u -> 10u 16V X7R
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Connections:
- C1 pad 1: +5V -> /Controller/PICO_5V
- C10 pad 1: +5V -> Net-(C10-Pad1)
- C11 pad 1: Net-(U5-EN) -> +5V
- C12 pad 1: Net-(U5-C+) -> Net-(U6-SENSE)
- C12 pad 2: Net-(U5-C-) -> GND
- C13 pad 1: GND -> +5V
- C13 pad 2: Net-(U5-CPOUT) -> GND
- C14 pad 1: GND -> +5V
- C14 pad 2: -4V_A -> GND
- C15 pad 1: +13V5 -> +5V
- C15 pad 2: Net-(U4-FB) -> GND
- C16 pad 1: +13V5 -> +3V3_C
- C17 pad 1: +13V5 -> +3V3_A
- C18 pad 1: Net-(U7-SET) -> +5V
- C19 pad 1: +12V_A -> Net-(U11-C+)
- C19 pad 2: GND -> Net-(U11-C-)
- C2 pad 1: +5V -> Net-(D2-A1)
- C20 pad 1: +13V5 -> Net-(U12-Vin)
- C21 pad 1: Net-(U6-Trim/NR) -> Net-(U11-VIN)
- C22 pad 1: VREF -> GND
- C22 pad 2: GND -> Net-(U11-CPOUT)
- C23 pad 1: +12V_A -> +13V5
- C23 pad 2: GND -> Net-(U10-FB)
- C24 pad 1: +5V -> Net-(U12-Trim/NR)
- C25 pad 1: +3V3_A -> +13V5
- C26 pad 1: +5V -> Net-(C26-Pad1)
- C27 pad 1: VREF -> +13V5
- C28 pad 1: +5V -> GND
- C28 pad 2: GND -> -4V_A
- C29 pad 1: +12V_A -> Net-(C29-Pad1)
- C3 pad 1: +5V -> Net-(D2-A1)
- C30 pad 1: GND -> Net-(U13-SET)
- C30 pad 2: -4V_A -> GND
- C31 pad 1: +3V3_A -> +12V_A
- C32 pad 1: Net-(C32-Pad1) -> Net-(U14C--)
- C33 pad 1: Net-(U11-+) -> Net-(U14A--)
- C34 pad 1: Net-(C32-Pad1) -> Net-(U14B--)
- C35 pad 1: Net-(C32-Pad1) -> +3V3_C
- C36 pad 1: Net-(C36-Pad1) -> +3V3_A
- C37 pad 1: Net-(U12-V_{CONTROL}) -> Net-(U16-PS/SYNC)
- C38 pad 1: Net-(U12-SET) -> Net-(U15-Vref)
- C39 pad 1: /Path Switching/LDO_OUT -> +5V
- C4 pad 1: +5V -> Net-(U4-dV/dT)
- C40 pad 1: /Path Switching/LDO_OUT -> +5V
- C41 pad 1: +12V_A -> Net-(U17-+)
- C42 pad 1: +12V_A -> Net-(C42-Pad1)
- C43 pad 1: Net-(U14-+) -> Net-(D11-K)
- C43 pad 2: GND -> Net-(C43-Pad2)
- C44 pad 1: +3V3_A -> +12V_A
- C45 pad 1: /Path Switching/SUPPLY -> Net-(C42-Pad1)
- C46 pad 1: +12V_A -> Net-(D11-K)
- C47 pad 1: +12V_A -> Net-(D10-K)
- C48 pad 1: +12V_A -> GND
- C48 pad 2: GND -> -4V_A
- C49 pad 1: +12V_A -> Net-(U18-SET)
- C5 pad 1: +5V -> Net-(C5-Pad1)
- C50 pad 1: GND -> Net-(C42-Pad1)
- C50 pad 2: -4V_A -> GND
- C51 pad 1: +12V_A -> +3V3_A
- C52 pad 1: +12V_A -> Net-(U19--)
- C52 pad 2: GND -> Net-(U16-FB)
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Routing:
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- added copper zone on In1.Cu, net GND
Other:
- board size 130 x 100 mm -> 150 x 100 mm
- board text added: "1 A branch"
- board text added: "5V IN 4.5-5.5V"
- board text added: "Front end"
- board text added: "GND = USB GND"
- board text added: "Gate drivers"
- board text added: "LOGIC PORT"
- board text added: "Output switch"
- board text added: "Power Profiler - Carrier Board rev A2 draft"
- board text added: "Reference"
- board text added: "USB DATA/POWER"
- board text added: "USB POWER ONLY"
- board text added: "VIN 0.8-5 V, 20 V max"
- board text added: "VIN entry"
- board text added: "VOUT 0.8-5 V,"
- board text added: "no reverse polarity"
- board text removed: "5V IN"
- board text removed: "Output"
- board text removed: "Power Profiler - Carrier Board rev A1 draft"
- board text removed: "Shunt ladder"
- board text removed: "Signal chain"
